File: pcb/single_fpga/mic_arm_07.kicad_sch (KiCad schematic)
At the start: 17 parts, among them U106 CDCLVC1108PW, U57 IM72D128V01XTMA1, U58 IM72D128V01XTMA1, U59 IM72D128V01XTMA1, U60 IM72D128V01XTMA1, U61 IM72D128V01XTMA1, U62 IM72D128V01XTMA1, U63 IM72D128V01XTMA1, U64 IM72D128V01XTMA1

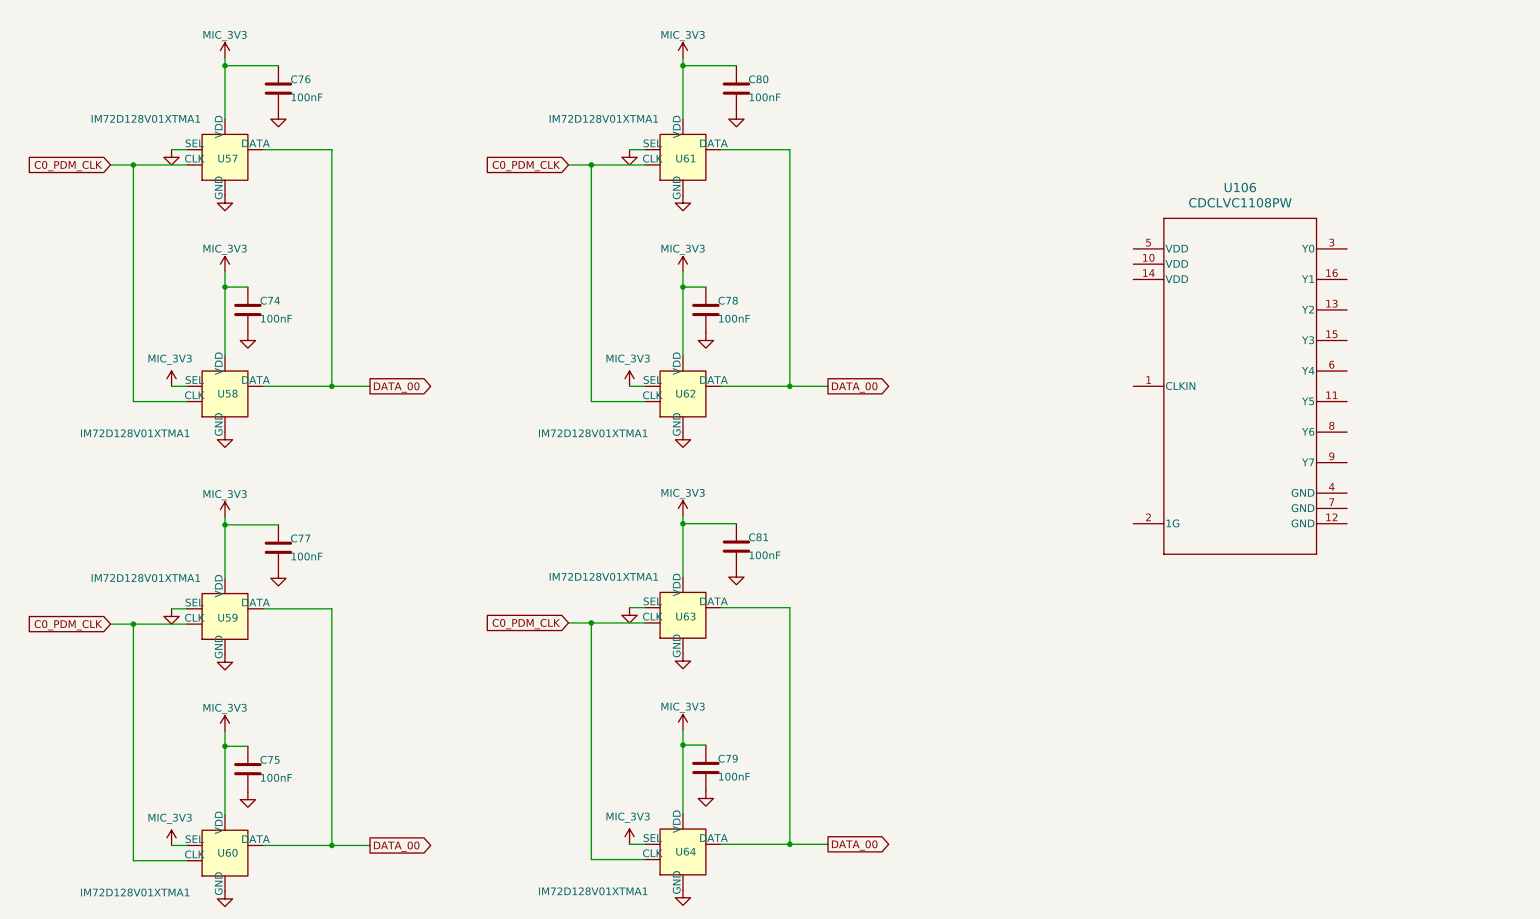
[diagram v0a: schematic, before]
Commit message: Fixed clocks and names.
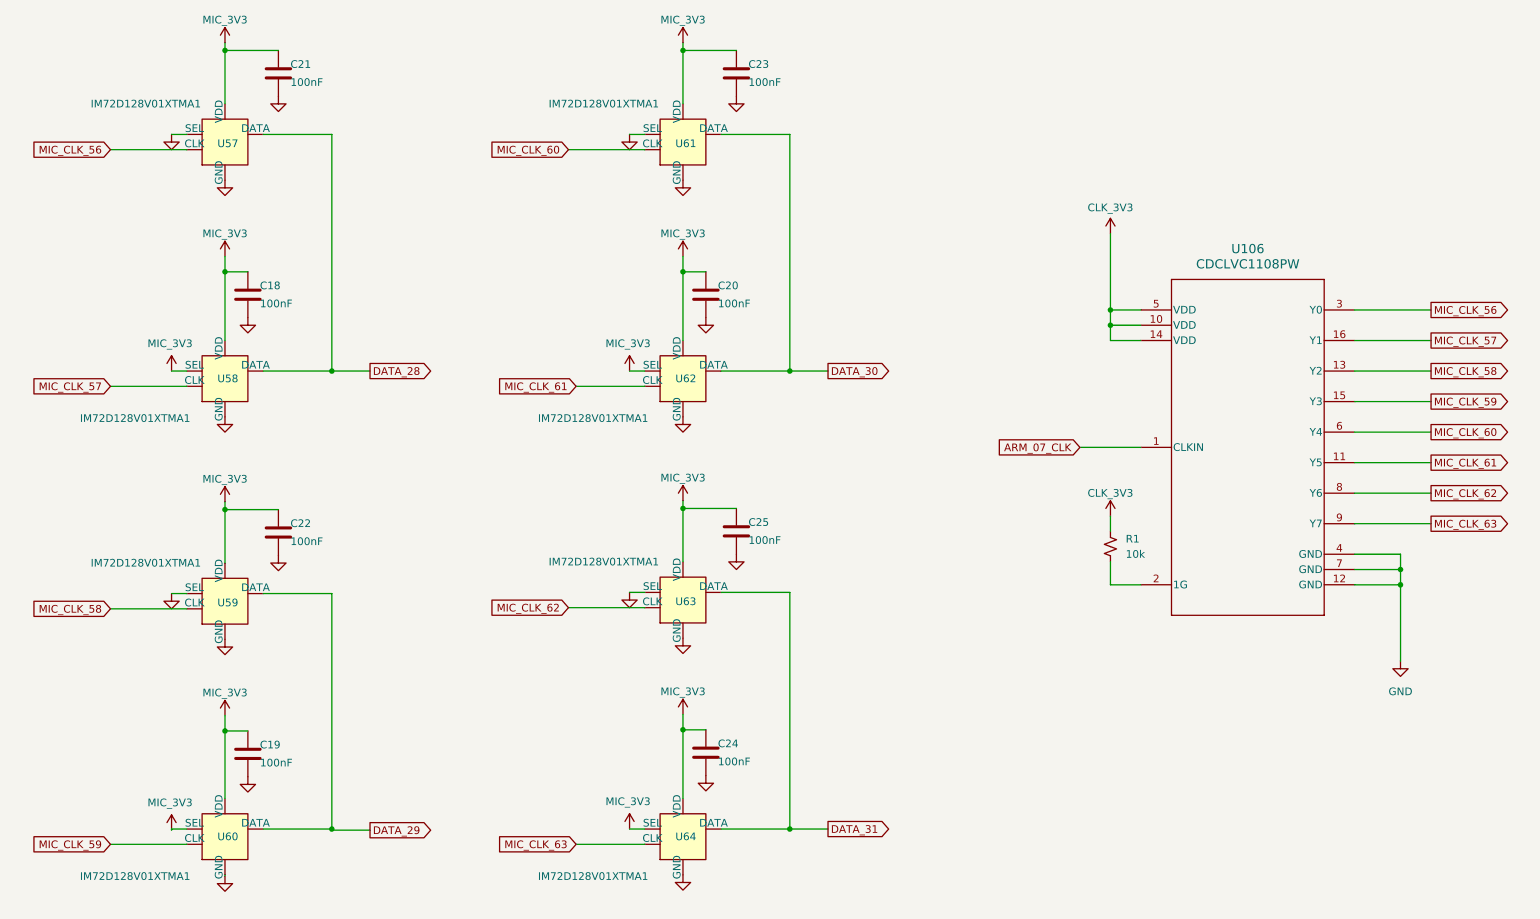
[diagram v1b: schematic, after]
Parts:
- removed C74, C75, C76, C77, C78, C79, C80, C81: 100nF, Capacitor_SMD:C_0603_1608Metric, symbol Device:C
- added C18, C19, C20, C21, C22, C23, C24, C25: 100nF, Capacitor_SMD:C_0603_1608Metric, symbol Device:C
- added R1: 10k, PCM_SparkFun-Resistor:R_0603_1608Metric, symbol PCM_SparkFun-Resistor:10k_0603
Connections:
- net GND: now also U106.12 (GND), U106.4 (GND), U106.7 (GND), C18.2, C19.2, C20.2, C21.2, C22.2, C23.2, C24.2, C25.2
- net MIC_3V3: now also C18.1, C19.1, C20.1, C21.1, C22.1, C23.1, C24.1, C25.1
- net ARM_07_CLK: now reaches U106.1 (CLKIN)
- net CLK_3V3: now reaches U106.10 (VDD)
- net CLK_3V3: now also U106.14 (VDD), U106.5 (VDD), R1.2
- net MIC_CLK_61: now reaches U106.11 (Y5)
- net MIC_CLK_61: now also U62.3 (CLK)
- net MIC_CLK_58: now reaches U106.13 (Y2)
- net MIC_CLK_58: now also U59.3 (CLK)
- net MIC_CLK_59: now reaches U106.15 (Y3)
- net MIC_CLK_59: now also U60.3 (CLK)
- net MIC_CLK_57: now reaches U106.16 (Y1)
- net MIC_CLK_57: now also U58.3 (CLK)
- net at U106.2 (1G): now also R1.1
- net MIC_CLK_56: now reaches U106.3 (Y0)
- net MIC_CLK_56: now also U57.3 (CLK)
- net MIC_CLK_60: now reaches U106.6 (Y4)
- net MIC_CLK_60: now also U61.3 (CLK)
- net MIC_CLK_62: now reaches U106.8 (Y6)
- net MIC_CLK_62: now also U63.3 (CLK)
- net MIC_CLK_63: now reaches U106.9 (Y7)
- net MIC_CLK_63: now also U64.3 (CLK)
- removed net C0_PDM_CLK: U57.3 (CLK), U58.3 (CLK), U59.3 (CLK), U60.3 (CLK), U61.3 (CLK), U62.3 (CLK), U63.3 (CLK), U64.3 (CLK)
- removed net DATA_00: U57.1 (DATA), U58.1 (DATA), U59.1 (DATA), U60.1 (DATA), U61.1 (DATA), U62.1 (DATA), U63.1 (DATA), U64.1 (DATA)
- new net DATA_28: U57.1 (DATA), U58.1 (DATA)
- new net DATA_29: U59.1 (DATA), U60.1 (DATA)
- new net DATA_30: U61.1 (DATA), U62.1 (DATA)
- new net DATA_31: U63.1 (DATA), U64.1 (DATA)

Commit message: Fixed all duplicate refdes's.
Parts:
- renumbered C18 to C74, C19 to C75, C20 to C76, C21 to C77, C22 to C78, C23 to C79, C24 to C80, C25 to C81, R1 to R12

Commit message: Fixed symbol library references.
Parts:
- U106: footprint PW0016A_N -> CDCLVC1108:PW0016A_N

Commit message: Fixed footprints. Added missing mic. Relinked placed footprints.
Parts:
- U57, U58, U59, U60, U61, U62, U63, U64: footprint (none) -> IM72D128:IFX-PG-LLGA-5-4
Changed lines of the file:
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@@
 			)
 		)
-		(property "Footprint" ""
+		(property "Footprint" "IM72D128:IFX-PG-LLGA-5-4"
 			(at 59.69 160.02 0)
 			(hide yes)
@@
 			)
 		)
-		(property "Footprint" ""
+		(property "Footprint" "IM72D128:IFX-PG-LLGA-5-4"
 			(at 135.89 160.02 0)
 			(hide yes)
@@
 			)
 		)
-		(property "Footprint" ""
+		(property "Footprint" "IM72D128:IFX-PG-LLGA-5-4"
 			(at 59.69 83.82 0)
 			(hide yes)
@@
 			)
 		)
-		(property "Footprint" ""
+		(property "Footprint" "IM72D128:IFX-PG-LLGA-5-4"
 			(at 59.69 120.65 0)
 			(hide yes)
@@
 			)
 		)
-		(property "Footprint" ""
+		(property "Footprint" "IM72D128:IFX-PG-LLGA-5-4"
 			(at 59.69 44.45 0)
 			(hide yes)
@@
 			)
 		)
-		(property "Footprint" ""
+		(property "Footprint" "IM72D128:IFX-PG-LLGA-5-4"
 			(at 135.89 83.82 0)
 			(hide yes)
@@
 			)
 		)
-		(property "Footprint" ""
+		(property "Footprint" "IM72D128:IFX-PG-LLGA-5-4"
 			(at 135.89 44.45 0)
 			(hide yes)
@@
 			)
 		)
-		(property "Footprint" ""
+		(property "Footprint" "IM72D128:IFX-PG-LLGA-5-4"
 			(at 135.89 120.65 0)
 			(hide yes)

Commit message: Updated all refdes's.
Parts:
- renumbered C74 to C57, C75 to C58, C77 to C59, C78 to C60, C76 to C61, C80 to C62, C79 to C63, C81 to C64, R12 to R8, U57 to U64, U58 to U65, U59 to U66, U60 to U67, U61 to U68, U62 to U69, U63 to U70, U64 to U71, U106 to U72

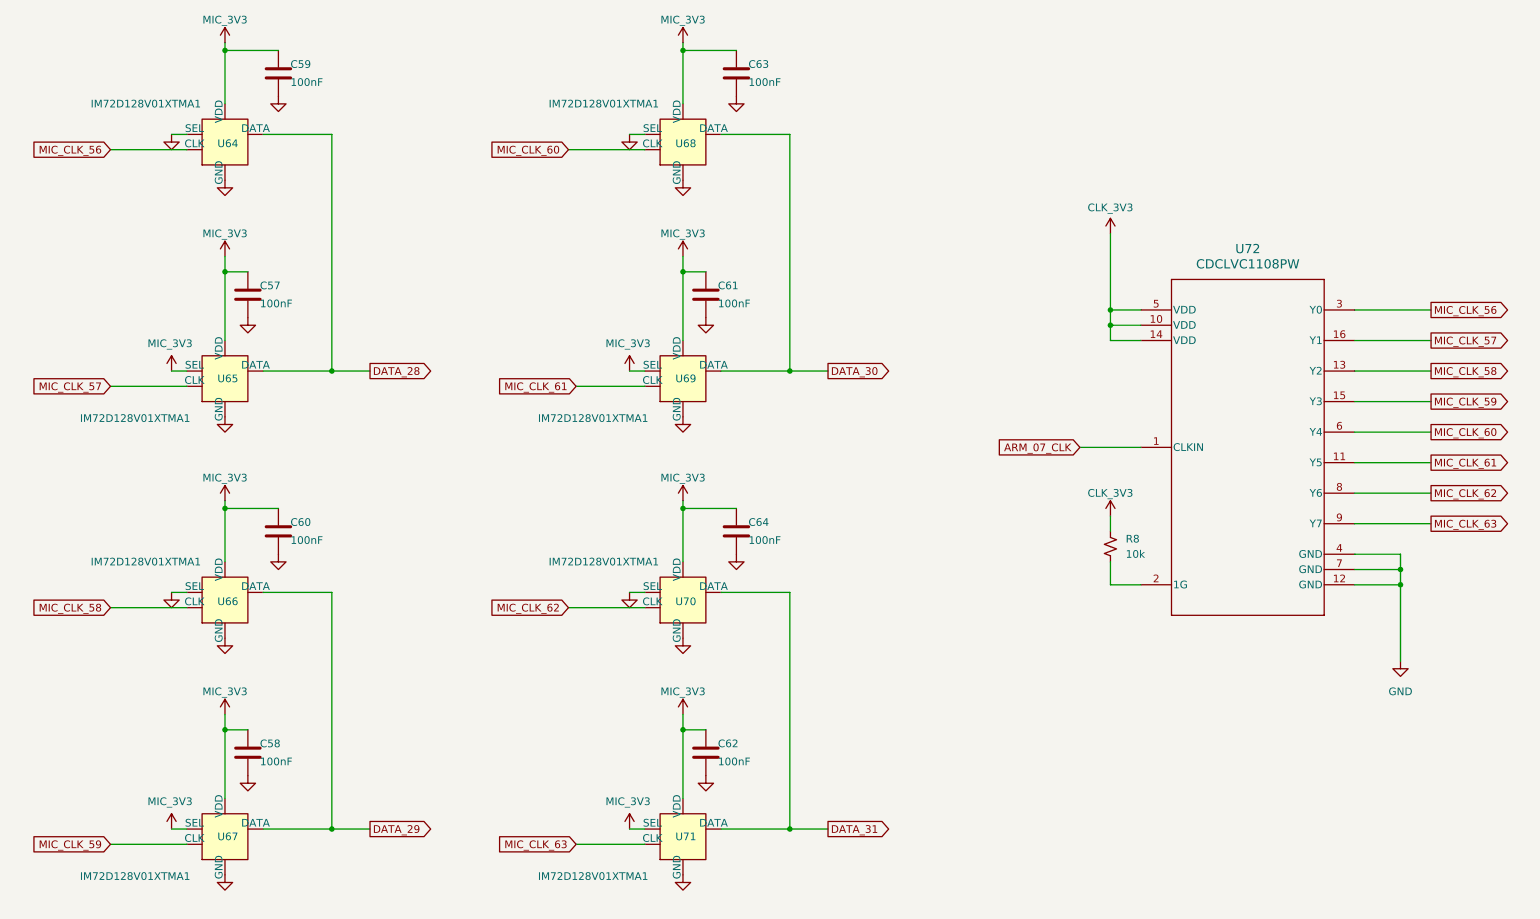
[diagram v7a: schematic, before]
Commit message: Changed mic symbol to improve readability.
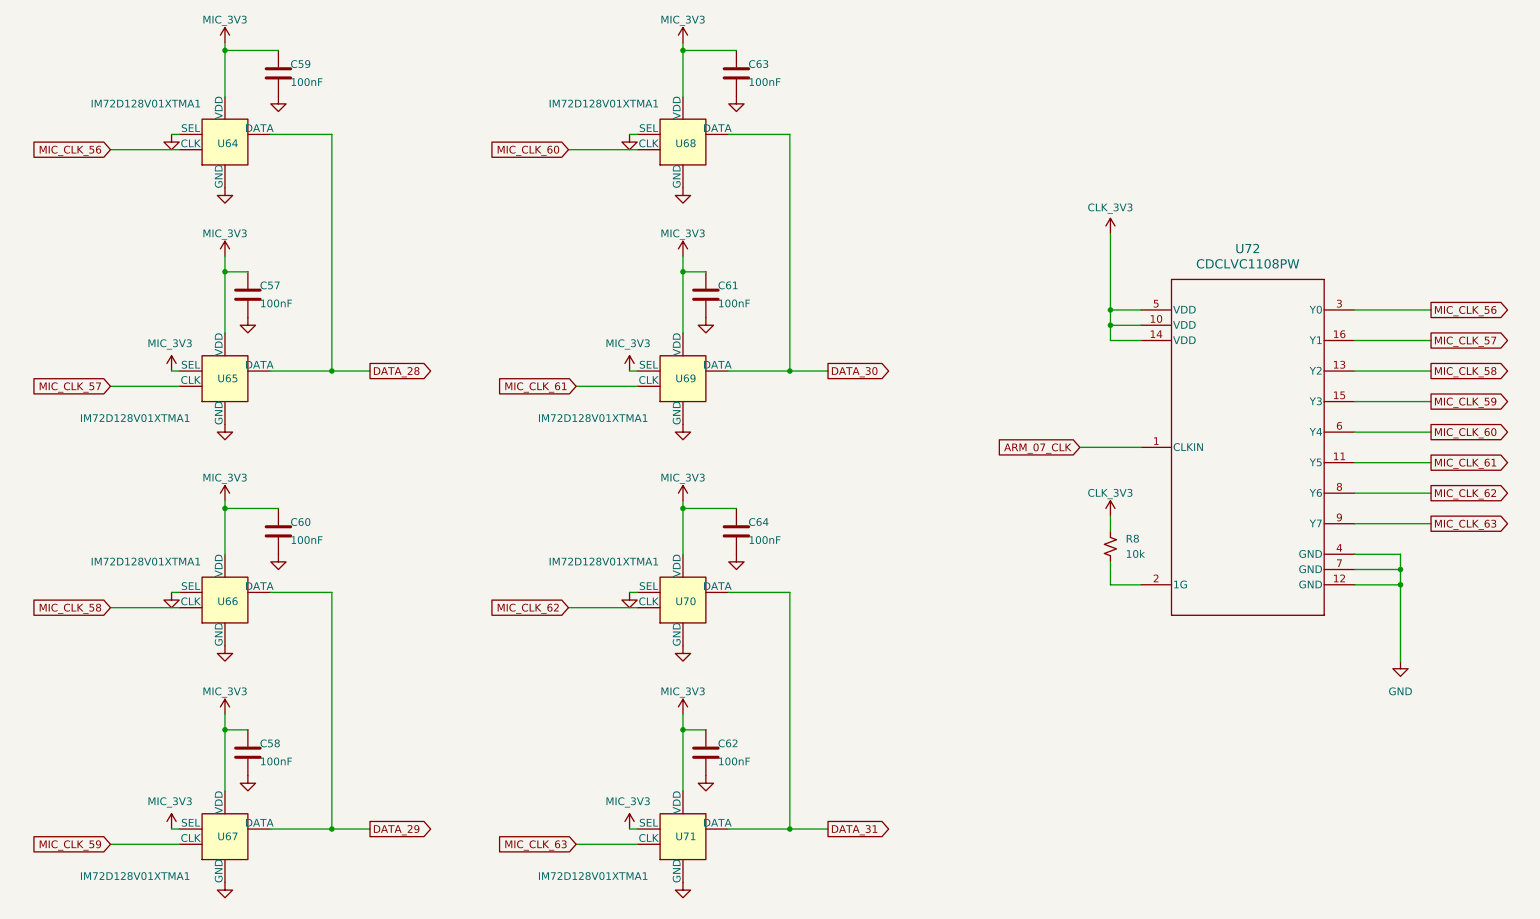
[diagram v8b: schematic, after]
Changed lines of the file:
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@@
 	(wire
 		(pts
-			(xy 77.47 119.38) (xy 66.04 119.38)
+			(xy 77.47 119.38) (xy 67.31 119.38)
 		)
 		(stroke
@@
 	(wire
 		(pts
-			(xy 118.11 161.29) (xy 129.54 161.29)
+			(xy 118.11 161.29) (xy 128.27 161.29)
 		)
 		(stroke
@@
 	(wire
 		(pts
-			(xy 50.8 119.38) (xy 53.34 119.38)
+			(xy 50.8 119.38) (xy 52.07 119.38)
 		)
 		(stroke
@@
 	(wire
 		(pts
-			(xy 50.8 82.55) (xy 53.34 82.55)
+			(xy 50.8 82.55) (xy 52.07 82.55)
 		)
 		(stroke
@@
 	(wire
 		(pts
-			(xy 50.8 43.18) (xy 53.34 43.18)
+			(xy 50.8 43.18) (xy 52.07 43.18)
 		)
 		(stroke
@@
 	(wire
 		(pts
-			(xy 135.89 105.41) (xy 135.89 114.3)
+			(xy 135.89 105.41) (xy 135.89 113.03)
 		)
 		(stroke
@@
 	(wire
 		(pts
-			(xy 153.67 43.18) (xy 142.24 43.18)
+			(xy 153.67 43.18) (xy 143.51 43.18)
 		)
 		(stroke
@@
 	(wire
 		(pts
-			(xy 135.89 142.24) (xy 135.89 153.67)
+			(xy 135.89 142.24) (xy 135.89 152.4)
 		)
 		(stroke
@@
 	(wire
 		(pts
-			(xy 118.11 85.09) (xy 129.54 85.09)
+			(xy 118.11 85.09) (xy 128.27 85.09)
 		)
 		(stroke
@@
 	(wire
 		(pts
-			(xy 59.69 29.21) (xy 59.69 38.1)
+			(xy 59.69 29.21) (xy 59.69 36.83)
 		)
 		(stroke
@@
 	(wire
 		(pts
-			(xy 40.64 161.29) (xy 53.34 161.29)
+			(xy 40.64 161.29) (xy 52.07 161.29)
 		)
 		(stroke
@@
 	(wire
 		(pts
-			(xy 116.84 121.92) (xy 129.54 121.92)
+			(xy 116.84 121.92) (xy 128.27 121.92)
 		)
 		(stroke
@@
 	(wire
 		(pts
-			(xy 59.69 66.04) (xy 59.69 77.47)
+			(xy 59.69 66.04) (xy 59.69 76.2)
 		)
 		(stroke
@@
 	(wire
 		(pts
-			(xy 40.64 85.09) (xy 53.34 85.09)
+			(xy 40.64 85.09) (xy 52.07 85.09)
 		)
 		(stroke
@@
 	(wire
 		(pts
-			(xy 116.84 45.72) (xy 129.54 45.72)
+			(xy 116.84 45.72) (xy 128.27 45.72)
 		)
 		(stroke
@@
 	(wire
 		(pts
-			(xy 142.24 158.75) (xy 153.67 158.75)
+			(xy 143.51 158.75) (xy 153.67 158.75)
 		)
 		(stroke
@@
 	(wire
 		(pts
-			(xy 40.64 121.92) (xy 53.34 121.92)
+			(xy 40.64 121.92) (xy 52.07 121.92)
 		)
 		(stroke
@@
 	(wire
 		(pts
-			(xy 153.67 119.38) (xy 142.24 119.38)
+			(xy 153.67 119.38) (xy 143.51 119.38)
 		)
 		(stroke
@@
 	(wire
 		(pts
-			(xy 127 43.18) (xy 129.54 43.18)
+			(xy 127 43.18) (xy 128.27 43.18)
 		)
 		(stroke
@@
 	(wire
 		(pts
-			(xy 142.24 82.55) (xy 153.67 82.55)
+			(xy 143.51 82.55) (xy 153.67 82.55)
 		)
 		(stroke
@@
 	(wire
 		(pts
-			(xy 135.89 66.04) (xy 135.89 77.47)
+			(xy 135.89 66.04) (xy 135.89 76.2)
 		)
 		(stroke
@@
 	(wire
 		(pts
-			(xy 127 158.75) (xy 129.54 158.75)
+			(xy 127 158.75) (xy 128.27 158.75)
 		)
 		(stroke
@@
 	(wire
 		(pts
-			(xy 127 119.38) (xy 129.54 119.38)
+			(xy 127 119.38) (xy 128.27 119.38)
 		)
 		(stroke
@@
 	(wire
 		(pts
-			(xy 66.04 82.55) (xy 77.47 82.55)
+			(xy 67.31 82.55) (xy 77.47 82.55)
 		)
 		(stroke
@@
 	(wire
 		(pts
-			(xy 40.64 45.72) (xy 53.34 45.72)
+			(xy 40.64 45.72) (xy 52.07 45.72)
 		)
 		(stroke
@@
 	(wire
 		(pts
-			(xy 135.89 29.21) (xy 135.89 38.1)
+			(xy 135.89 29.21) (xy 135.89 36.83)
 		)
 		(stroke
@@
 	(wire
 		(pts
-			(xy 77.47 43.18) (xy 66.04 43.18)
+			(xy 77.47 43.18) (xy 67.31 43.18)
 		)
 		(stroke
@@
 	(wire
 		(pts
-			(xy 59.69 142.24) (xy 59.69 153.67)
+			(xy 59.69 142.24) (xy 59.69 152.4)
 		)
 		(stroke
@@
 	(wire
 		(pts
-			(xy 127 82.55) (xy 129.54 82.55)
+			(xy 127 82.55) (xy 128.27 82.55)
 		)
 		(stroke
@@
 	(wire
 		(pts
-			(xy 66.04 158.75) (xy 77.47 158.75)
+			(xy 67.31 158.75) (xy 77.47 158.75)
 		)
 		(stroke
@@
 	(wire
 		(pts
-			(xy 59.69 105.41) (xy 59.69 114.3)
+			(xy 59.69 105.41) (xy 59.69 113.03)
 		)
 		(stroke
@@
 	(wire
 		(pts
-			(xy 50.8 158.75) (xy 53.34 158.75)
+			(xy 50.8 158.75) (xy 52.07 158.75)
 		)
 		(stroke
@@
 	(symbol
 		(lib_id "power:GND")
-		(at 135.89 166.37 0)
+		(at 135.89 167.64 0)
 		(unit 1)
 		(body_style 1)
@@
 	(symbol
 		(lib_id "power:GND")
-		(at 59.69 127 0)
+		(at 59.69 128.27 0)
 		(unit 1)
 		(body_style 1)
@@
 	(symbol
 		(lib_id "power:GND")
-		(at 59.69 90.17 0)
+		(at 59.69 91.44 0)
 		(unit 1)
 		(body_style 1)
@@
 	(symbol
 		(lib_id "power:GND")
-		(at 135.89 127 0)
+		(at 135.89 128.27 0)
 		(unit 1)
 		(body_style 1)
@@
 	(symbol
 		(lib_id "power:GND")
-		(at 135.89 50.8 0)
+		(at 135.89 52.07 0)
 		(unit 1)
 		(body_style 1)
@@
 	(symbol
 		(lib_id "power:GND")
-		(at 59.69 50.8 0)
+		(at 59.69 52.07 0)
 		(unit 1)
 		(body_style 1)
@@
 	(symbol
 		(lib_id "power:GND")
-		(at 59.69 166.37 0)
+		(at 59.69 167.64 0)
 		(unit 1)
 		(body_style 1)
@@
 	(symbol
 		(lib_id "power:GND")
-		(at 135.89 90.17 0)
+		(at 135.89 91.44 0)
 		(unit 1)
 		(body_style 1)
